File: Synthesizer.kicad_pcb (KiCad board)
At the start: 6 copper layers, 163 parts, among them J1 USB_A, J2 AudioJack3, J3 USB_B_Micro, J4 FPGA_debug, J5 MCU_debug, J6 67997-410HLF, SW1 SW_Push, SW10 SW_Push, SW11 SW_Push, SW12 SW_Push, SW13 SW_Push, SW14 SW_Push, SW15 SW_Push, SW16 SW_Push, SW2 SW_Push, SW3 SW_Push, SW4 SW_Push, SW5 SW_Push, SW6 SW_Push, SW7 SW_Push, SW8 SW_Push, SW9 SW_Push, U1 TPD3S014, U2 S25FL127S, U3 XC7A100T-FTG256, U4 Oscillator, U5 TPS54325, U6 TPS54294, U7 EFM32GG11B4xx, U8 PCM5102, Y1 48Mhz

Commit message: Rearrange PCB components to more closely match schematics and take up less space
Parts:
- J6: value 67997-410HLF -> MCU_GPIO
- R33, R34: value 15 -> 33
- moved U4 179.5 mm to (27.3, 92.1)
- moved C4 179.4 mm to (32.4, 91.8)
- moved R4 167.9 mm to (50.2, 119.1)
- moved J4 164.6 mm to (59.7, 126.4)
- moved R3 163.3 mm to (33.3, 104.8)
- moved R7 163.1 mm to (59.7, 119.1)
- moved R1 162.1 mm to (33.4, 101.6)
- moved R2 162.1 mm to (47.0, 119.1)
- moved R5 161.0 mm to (53.3, 119.1)
- moved U2 153.7 mm to (25.4, 105.3), turned to 270 degrees
- moved J2 148.2 mm to (132.1, 103.5)
- moved C77 146.5 mm to (102.6, 97.2), turned to 0 degrees
- moved R8 137.9 mm to (33.4, 110.5), turned to 180 degrees
- moved C76 135.1 mm to (102.6, 86.4), turned to 180 degrees
- moved C73 128.7 mm to (102.5, 94.0), turned to 0 degrees
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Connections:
- C2 pad 2: Net-(C2-Pad2) -> +5V
- C73 pad 1: +3V3 -> GND
- C73 pad 2: GND -> +3V3
- D1 pad 2: /EFM32/GREEN_LED -> /EFM32/RED_LED
- J1 pad 2: /EFM32/USB_D- -> Net-(J1-Pad2)
- J1 pad 3: /EFM32/USB_D+ -> Net-(J1-Pad3)
- J3 pad 6: Net-(J3-Pad6) -> GND
- R33 pad 1: Net-(R33-Pad1) -> /EFM32/USB_D+
- R33 pad 2: /EFM32/USB_D- -> Net-(J1-Pad3)
- R34 pad 1: Net-(R34-Pad1) -> /EFM32/USB_D-
- R34 pad 2: /EFM32/USB_D+ -> Net-(J1-Pad2)
- U1 pad 3: Net-(C2-Pad2) -> +5V
- U1 pad 5: Net-(C1-Pad2) -> Net-(J1-Pad2)
- U1 pad 6: /EFM32/USB_D+ -> Net-(J1-Pad3)
- U7 pad 34: /EFM32/GREEN_LED -> /EFM32/RED_LED
- U7 pad 47: Net-(R33-Pad1) -> /EFM32/USB_D-
- U7 pad 48: Net-(R34-Pad1) -> /EFM32/USB_D+
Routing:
- net Net-(FB1-Pad1): track 0.00 -> 8.18 mm
- net GND: track 0.00 -> 6.06 mm, vias 0 -> 2
- net Net-(FB4-Pad1): track 0.00 -> 4.83 mm
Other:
- net class +5V internal added: clearance 0.15, trace_width 0.3, via_dia 0.6, via_drill 0.3

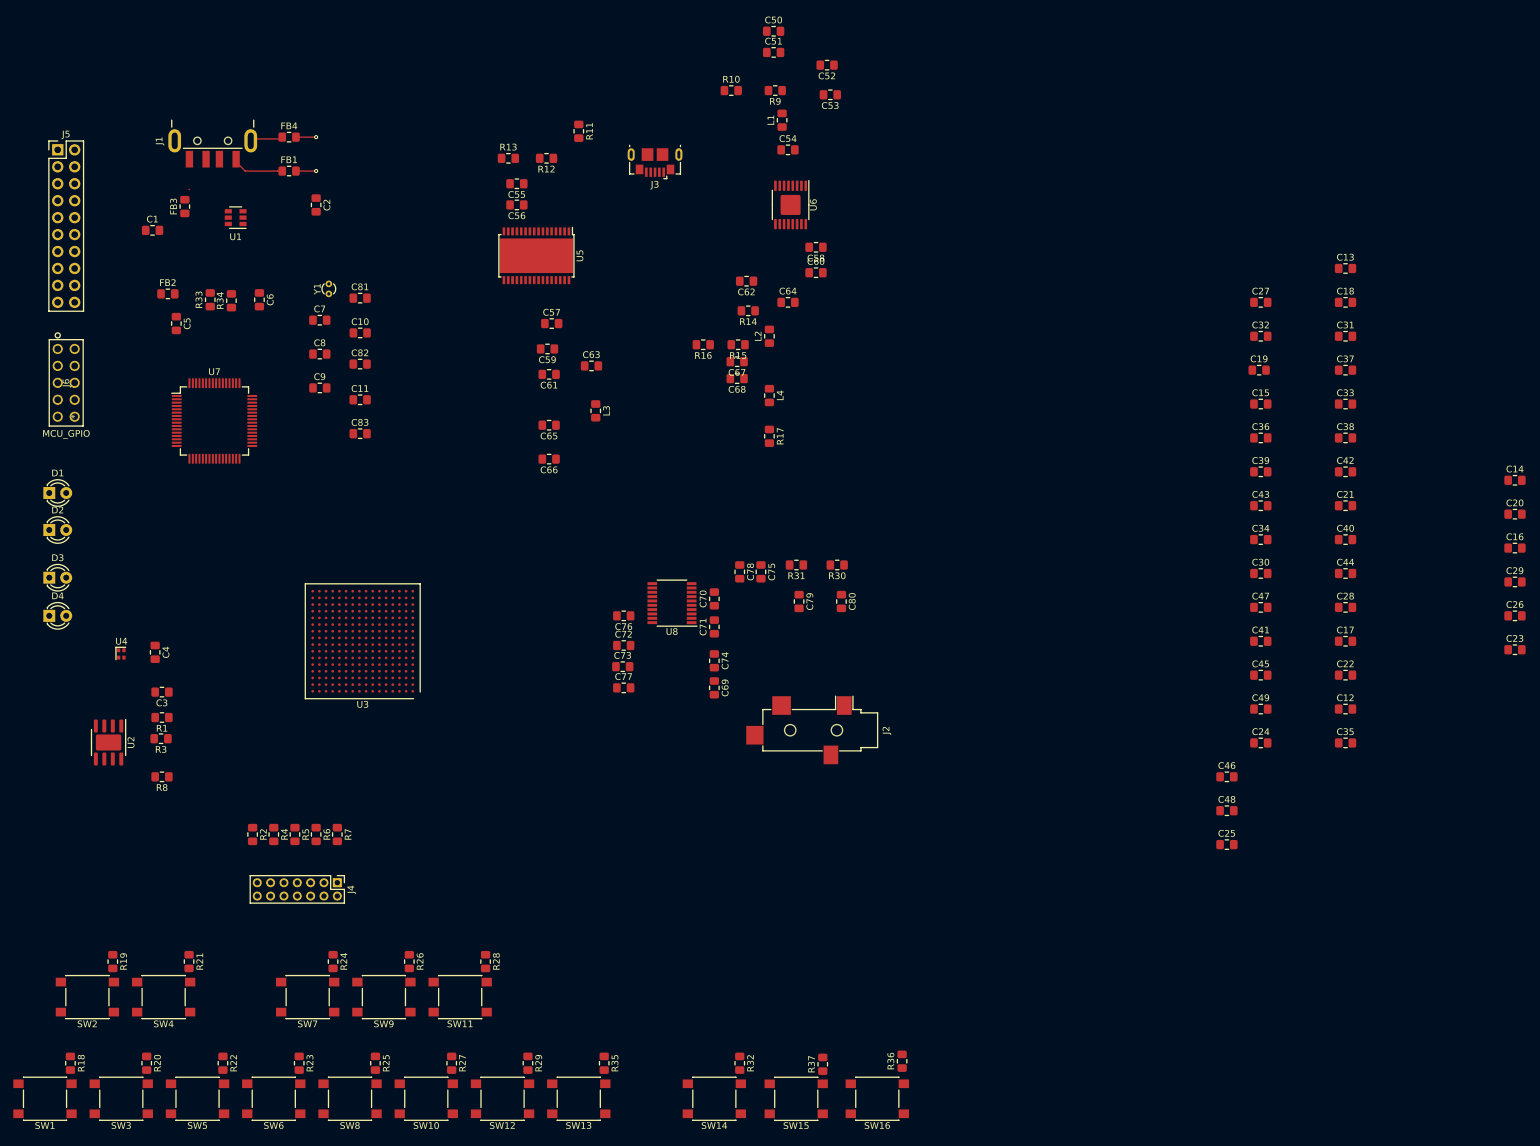
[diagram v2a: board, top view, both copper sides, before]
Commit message: Fixed u being written as µ (my bad.) Tried doing work on the PSU but it's eldritch.
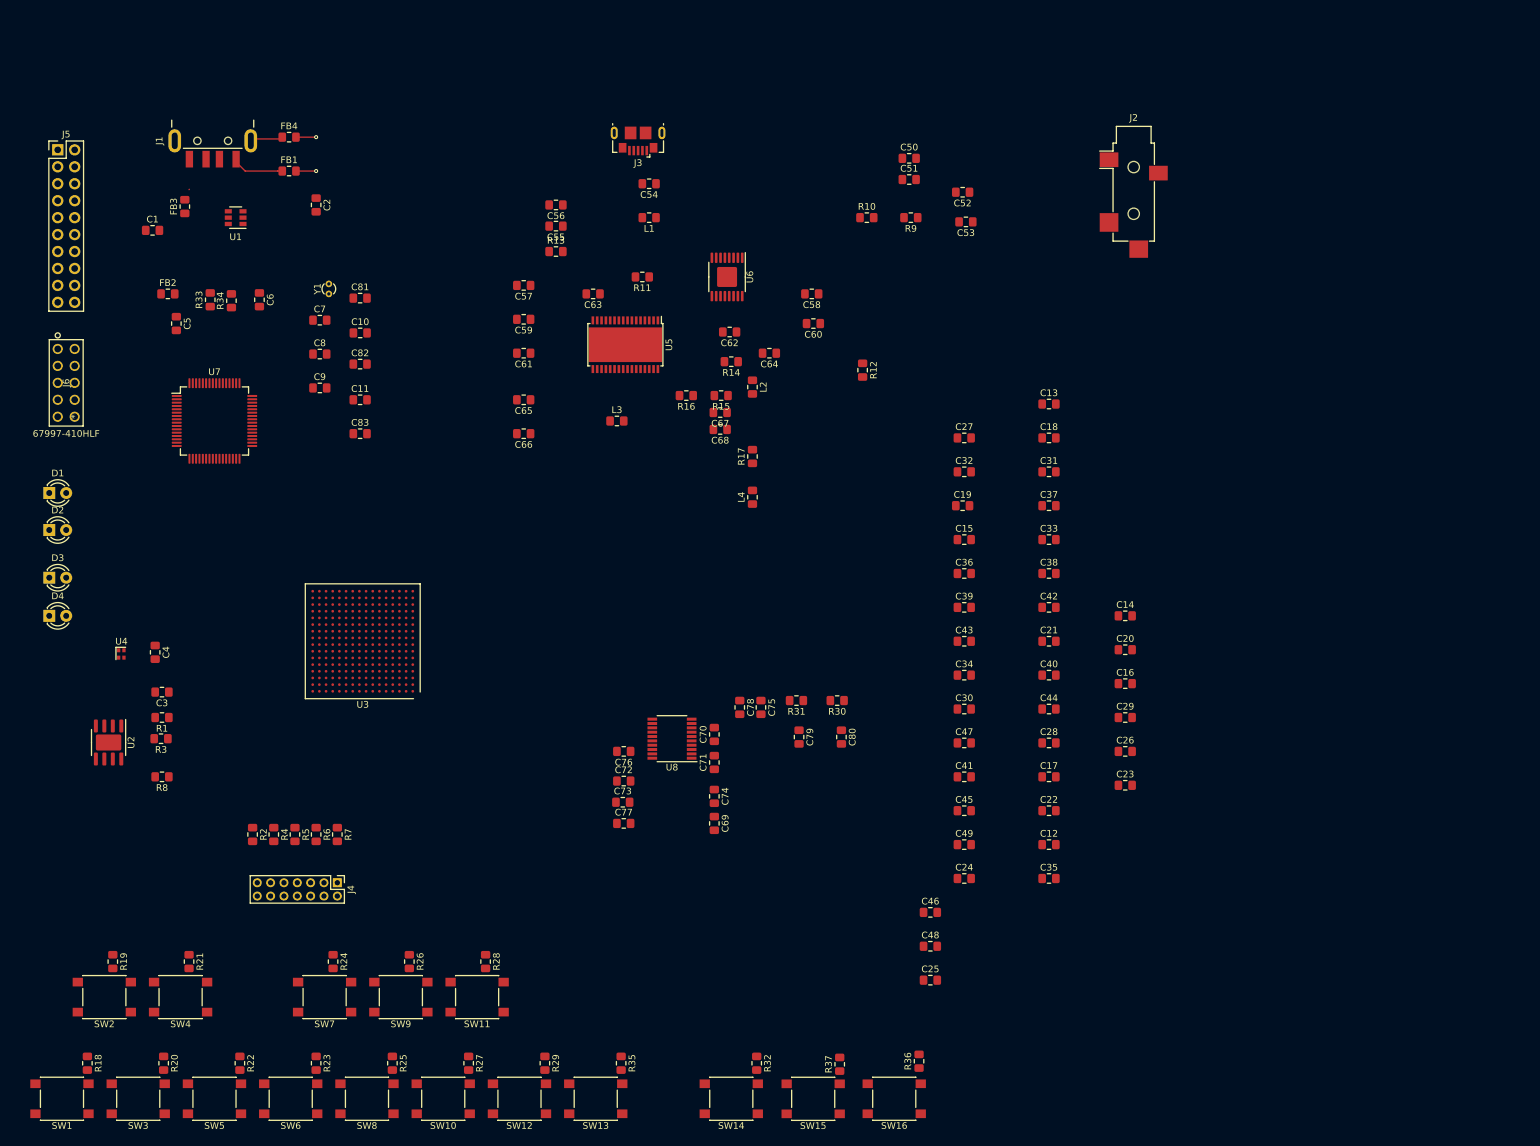
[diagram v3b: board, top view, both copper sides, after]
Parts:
- C50, C51, C67, C68: value 22µ -> 22u
- C62: value 1µ -> 1u
- J6: value MCU_GPIO -> 67997-410HLF
- moved J2 94.4 mm to (179.1, 21.6), turned to 0 degrees
- moved C14 61.9 mm to (177.8, 86.4)
- moved C16 61.9 mm to (177.8, 96.5)
- moved C20 61.9 mm to (177.8, 91.4)
- moved C23 61.9 mm to (177.8, 111.8)
- moved C26 61.9 mm to (177.8, 106.7)
- moved C29 61.9 mm to (177.8, 101.6)
- moved R12 57.0 mm to (138.4, 49.5), turned to 270 degrees
- moved C15 48.9 mm to (153.7, 74.9)
- moved C24 48.9 mm to (153.7, 125.7)
- moved C27 48.9 mm to (153.7, 59.7)
- moved C36 48.9 mm to (153.7, 80.0)
- moved C39 48.9 mm to (153.7, 85.1)
- moved C43 48.9 mm to (153.7, 90.2)
- moved C49 48.9 mm to (153.7, 120.7)
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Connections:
- D1 pad 1: GND -> Net-(D1-Pad1)
- D2 pad 1: GND -> Net-(D2-Pad1)
- D3 pad 1: GND -> Net-(D3-Pad1)
- D4 pad 1: GND -> Net-(D4-Pad1)
- J2 pad R: /Audio DAC/OUTR -> Net-(J2-PadR)
- J2 pad T: /Audio DAC/OUTL -> Net-(J2-PadT)
- U3 pad K13: /Audio DAC/Bit-clock -> /Artix7/IO_L5P_T0_D06_14
- U3 pad L14: /Artix7/IO_L4P_T0_D04_14 -> /Audio DAC/Bit-clock
- U7 pad 2: /Audio DAC/Soft-mute -> /EFM32/Soft-mute
- U7 pad 33: Net-(U7-Pad32) -> Net-(U7-Pad33)
- U8 pad 10: GND -> /Audio DAC/De-emphasis
- U8 pad 11: GND -> /Audio DAC/Filter-select
- U8 pad 12: /Artix7/IO_L5P_T0_D07_14 -> /Audio DAC/System-master-clock
- U8 pad 15: /Artix7/IO_L4P_T0_D04_14 -> /Artix7/IO_L5P_T0_D06_14
- U8 pad 16: GND -> /Audio DAC/Format-select

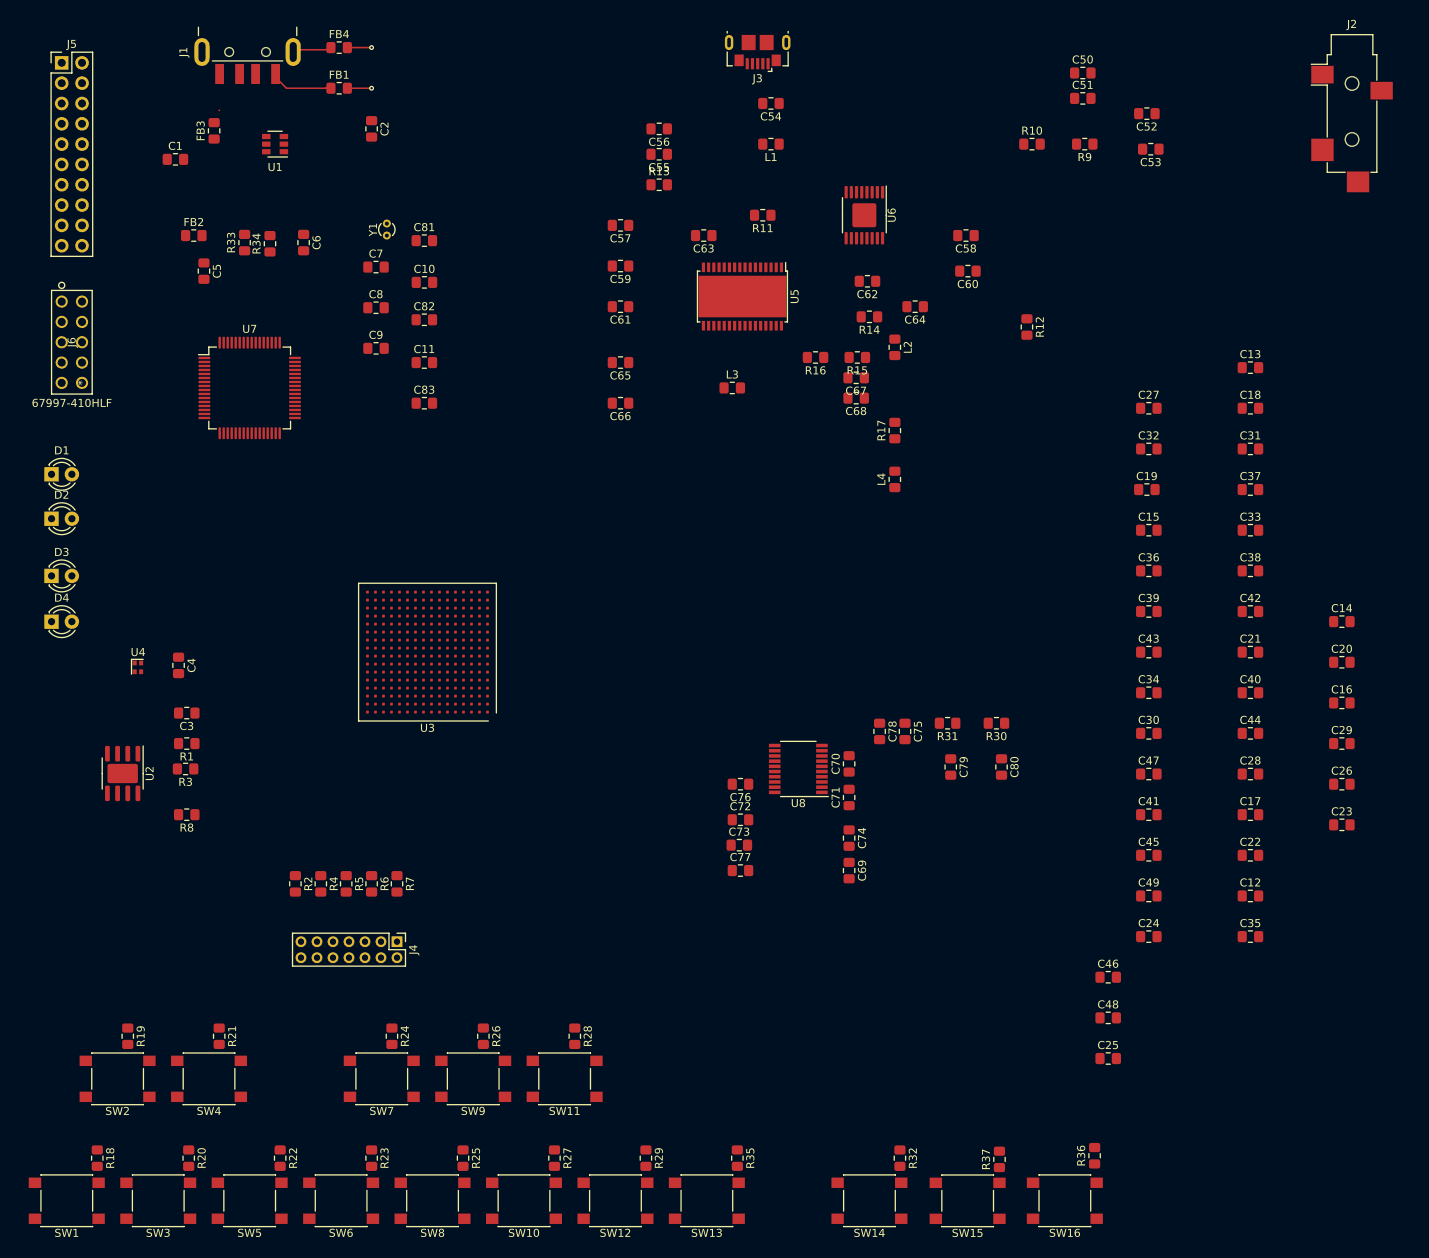
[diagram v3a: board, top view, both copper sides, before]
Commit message: Route tracks for buttons among other things
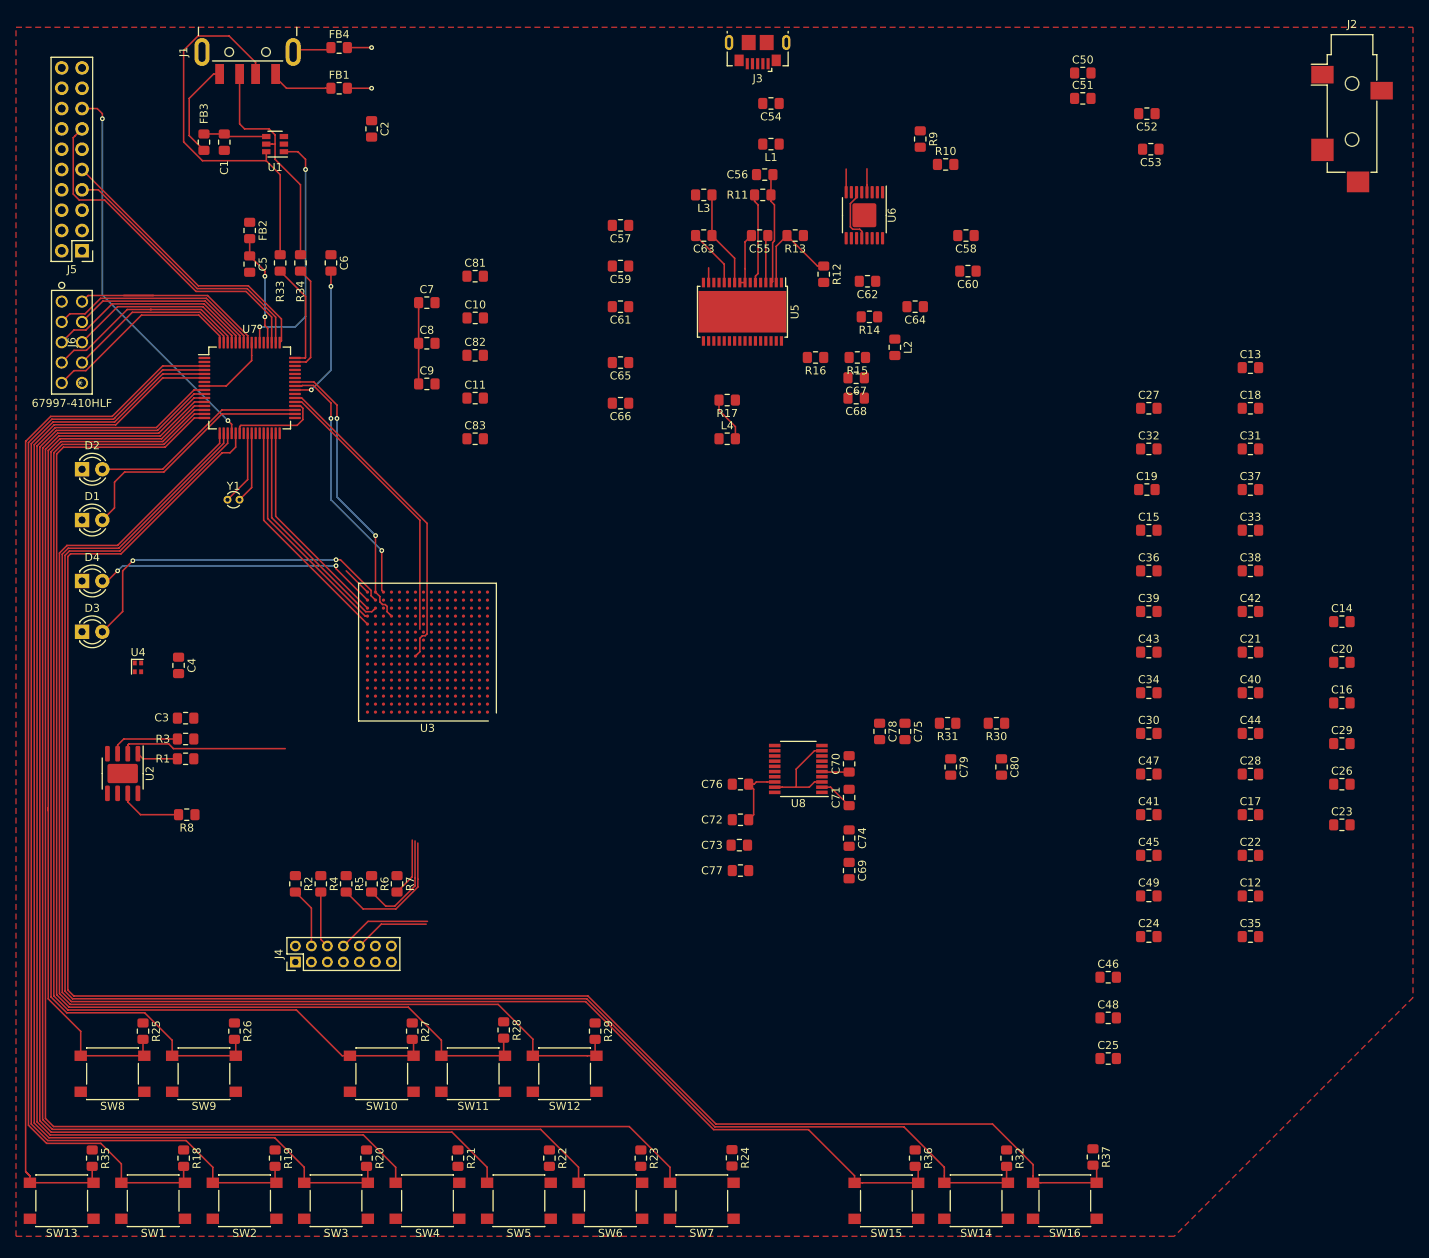
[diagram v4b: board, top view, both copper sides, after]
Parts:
- moved R35 80.6 mm to (21.6, 153.4)
- moved SW13 80.6 mm to (17.8, 158.8)
- moved R24 45.1 mm to (101.6, 153.4)
- moved SW8 43.0 mm to (24.1, 142.9)
- moved R25 43.0 mm to (27.9, 137.6)
- moved SW7 42.8 mm to (97.8, 158.8)
- moved Y1 38.6 mm to (38.5, 71.1), turned to 0 degrees
- moved SW9 33.7 mm to (35.6, 142.9)
- moved SW5 33.7 mm to (74.9, 158.8)
- moved R23 33.7 mm to (90.2, 153.4)
- moved SW6 33.7 mm to (86.4, 158.8)
- moved R22 33.7 mm to (78.7, 153.4)
- moved R21 33.5 mm to (67.3, 153.4)
- moved SW4 31.3 mm to (63.5, 158.8)
- moved R26 31.1 mm to (39.4, 137.6)
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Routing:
- net /Button15: track 0.00 -> 224.9 mm
- net /Button14: track 0.00 -> 212.9 mm
- net /Button13: track 0.00 -> 201.5 mm
- net /Button7: track 0.00 -> 188.5 mm
- net /Button6: track 0.00 -> 178.1 mm
- net /Button5: track 0.00 -> 167.8 mm
- net /Button3: track 0.00 -> 157.6 mm
- net /Button4: track 0.00 -> 157.4 mm
- net /Button12: track 0.00 -> 155.7 mm
- net /Button11: track 0.00 -> 150.5 mm
- net /Button2: track 0.00 -> 147.2 mm
- net /Button10: track 0.00 -> 138.9 mm
- net /Button1: track 0.00 -> 137.1 mm
- net /Button0: track 0.00 -> 129.9 mm
- net /Button9: track 0.00 -> 118.9 mm
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- added copper zone on F.Cu, net GND
